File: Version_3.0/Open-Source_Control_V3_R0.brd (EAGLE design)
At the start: 121.9 x 129.5 mm, 353 parts, among them IC10 MCP6002SMT, IC11 MCP6002SMT, IC12 MCP6002SMT, IC14 MCP6002SMT, IC2 ULN2003AD, IC4 74HC165D, IC5 74HC165D, J24 6p-2.54, K1 G5LE-14-CF DC24, K2 G5LE-14-CF DC24, K3 G5LE-14-CF DC24, K4 G5LE-14-CF DC24, Q1 MMBT2907, T4 DA2304-AL, U1 OSD3358-512M-ICB, U16 AT97SC3205T-G3M4400B, U2 TPD4S012_DRY_6_P1_M, U27 LAN8710, U28 TCAN1051HV, U29 MAX3483EESA+T, U4 APX811-31UGSOT, U40 ISO3086TDW, U5 TLVH431, U6 SN74LVC2G241_DCU_8, X1 10118194-0001LF, X10 MC4, X11 MC4, X12 MC4, X2 J0011D01BNL, X21 MC12, X24 MSTBA2, X3 MC4, X31 MC4, X4 CTI-JTAG, X41 MSTBA3, X5 DM3CS-SF, X6 6p-2.54, X7 TH-2X10, X8 TH-2X10, X9 5600200420, Y7 ECS-250-12-30-GN-TR

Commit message: Add files via upload
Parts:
- renumbered H4 to MTG4
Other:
- board text added: "Control v3"
- board text removed: "Building Control v3"
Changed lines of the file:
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@@
 <text x="50.8" y="0.635" size="1.016" layer="21" font="vector" ratio="12">Rev 0</text>
 <text x="40.64" y="4.318" size="1.27" layer="21" ratio="15">Open-Source</text>
-<text x="40.64" y="2.54" size="1.27" layer="21" ratio="15">Building Control v3</text>
+<text x="40.64" y="2.54" size="1.27" layer="21" ratio="15">Control v3</text>
 <wire x1="95.25" y1="107.95" x2="95.25" y2="102.87" width="0.4064" layer="21"/>
 <wire x1="95.25" y1="102.87" x2="90.17" y2="102.87" width="0.4064" layer="21"/>
@@
 </element>
 <element name="D402" library="OSD3358-SM-RED Platform" package="EIA-STD" value="LTST-C191KGKT" x="20.828" y="108.585" smashed="yes" rot="R90">
-<attribute name="NAME" x="20.8534" y="107.1372" size="0.8128" layer="25" align="top-center"/>
+<attribute name="NAME" x="20.828" y="110.0328" size="0.8128" layer="25" align="bottom-center"/>
 <attribute name="VALUE" x="20.1676" y="108.585" size="0.254" layer="27" rot="R90" align="bottom-center"/>
 </element>
 <element name="D401" library="OSD3358-SM-RED Platform" package="EIA-STD" value="LTST-C191KRKT" x="18.796" y="108.585" smashed="yes" rot="R90">
-<attribute name="NAME" x="18.796" y="107.1372" size="0.8128" layer="25" align="top-right"/>
+<attribute name="NAME" x="18.796" y="110.0328" size="0.8128" layer="25" align="bottom-right"/>
 <attribute name="VALUE" x="19.4564" y="108.585" size="0.254" layer="27" rot="R90" align="top-center"/>
 </element>
@@
 <attribute name="POPULARITY" value="0" x="36.195" y="125.095" size="1.778" layer="27" display="off"/>
 </element>
-<element name="H4" library="holes" library_urn="urn:adsk.eagle:library:237" package="3,6-PAD" package3d_urn="urn:adsk.eagle:package:14284/1" value="MOUNT-PAD-ROUND3.6" x="85.725" y="125.095" smashed="yes">
+<element name="MTG4" library="holes" library_urn="urn:adsk.eagle:library:237" package="3,6-PAD" package3d_urn="urn:adsk.eagle:package:14284/1" value="MOUNT-PAD-ROUND3.6" x="85.725" y="125.095" smashed="yes">
 <attribute name="POPULARITY" value="0" x="85.725" y="125.095" size="1.778" layer="27" display="off"/>
 </element>
@@
 <contactref element="MTG1" pad="B3,6"/>
 <contactref element="MTG2" pad="B3,6"/>
-<contactref element="H4" pad="B3,6"/>
+<contactref element="MTG4" pad="B3,6"/>
 <contactref element="MTG3" pad="B3,6"/>
 </signal>

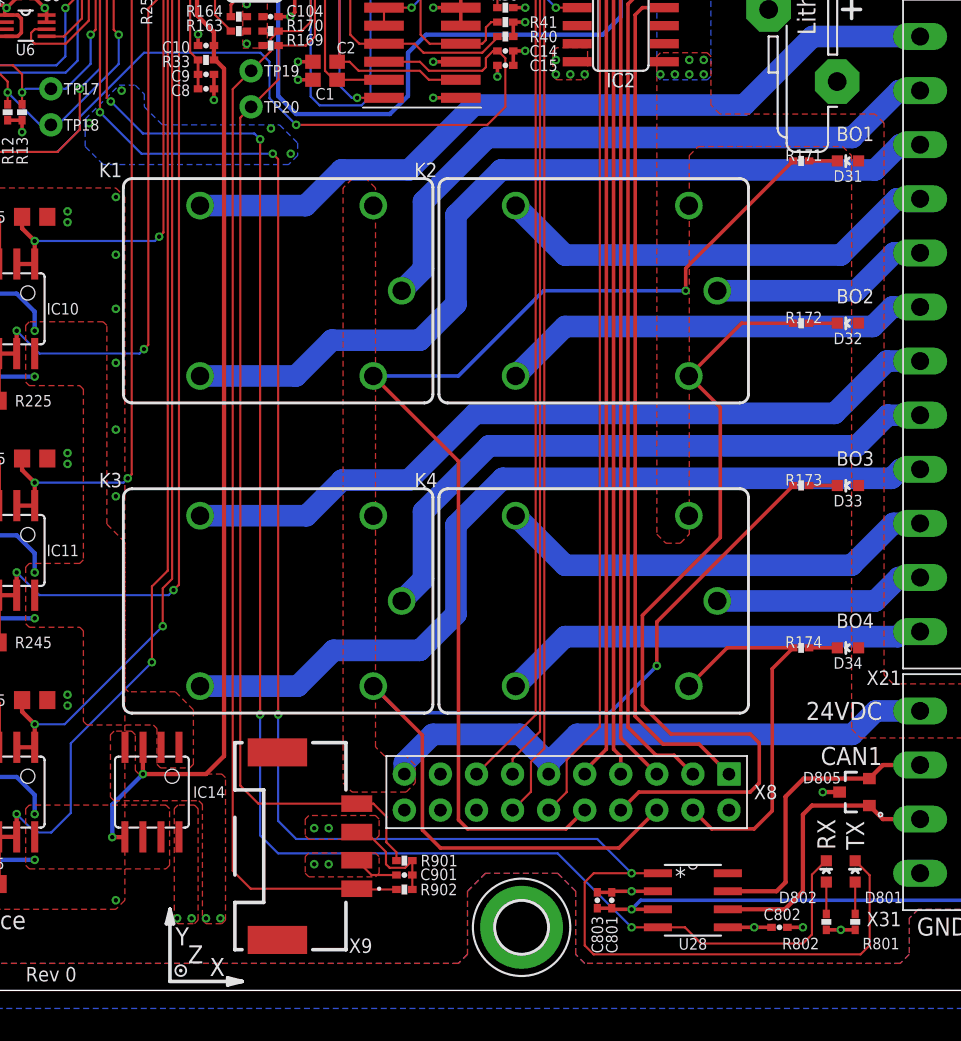
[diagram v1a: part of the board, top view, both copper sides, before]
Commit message: Add files via upload
Fixed CAN1_TXD CAN1_RXD criss-crossed
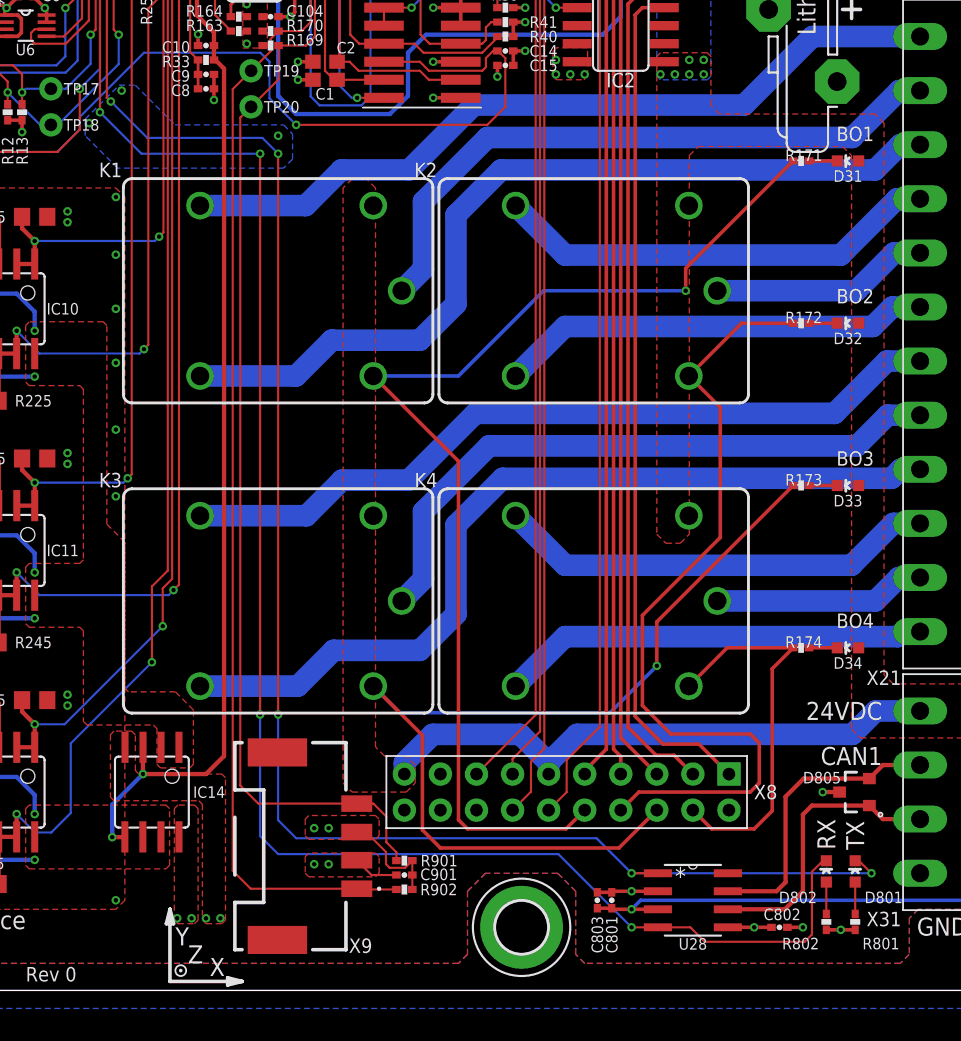
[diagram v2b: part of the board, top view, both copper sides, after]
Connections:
- net CAN1_RXD: now also U1.W7; no longer U1.Y7
- net CAN1_TXD: now also U1.Y7; no longer U1.W7
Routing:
- net CAN1_TXD: track 141.5 -> 122.5 mm, vias 4 -> 5
- net CAN1_RXD: track 124.2 -> 126.2 mm
- net GND: vias 198 -> 197
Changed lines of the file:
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@@
 <vertex x="70.739" y="9.6774"/>
 </polygon>
-<via x="68.072" y="60.706" extent="1-16" drill="0.3048"/>
+<via x="68.58" y="60.198" extent="1-16" drill="0.3048"/>
 <via x="55.2704" y="61.087" extent="1-16" drill="0.3048"/>
-<via x="69.469" y="58.928" extent="1-16" drill="0.3048"/>
 <wire x1="93.472" y1="6.985" x2="95.3262" y2="6.985" width="0.254" layer="1"/>
 <wire x1="93.472" y1="6.985" x2="92.1512" y2="6.985" width="0.254" layer="1"/>
@@
 <vertex x="57.3786" y="63.754"/>
 <vertex x="58.5216" y="63.754"/>
-<vertex x="59.1566" y="63.119"/>
-<vertex x="59.1566" y="62.23"/>
-<vertex x="60.4266" y="60.96"/>
-<vertex x="68.6816" y="60.96"/>
-<vertex x="69.9516" y="59.69"/>
-<vertex x="69.9516" y="58.801"/>
-<vertex x="69.3166" y="58.166"/>
-<vertex x="56.261" y="58.166"/>
-<vertex x="54.991" y="59.436"/>
+<vertex x="61.3156" y="60.96"/>
+<vertex x="68.961" y="60.96"/>
+<vertex x="69.596" y="60.325"/>
+<vertex x="69.596" y="58.547"/>
+<vertex x="68.961" y="57.912"/>
+<vertex x="57.277" y="57.912"/>
+<vertex x="54.991" y="60.198"/>
 <vertex x="54.991" y="61.3664"/>
 </polygon>
@@
 <wire x1="51.435" y1="67.69608125" x2="52.2732" y2="67.69608125" width="0.1524" layer="1"/>
 </signal>
-<signal name="CAN1_TXD">
-<contactref element="U28" pad="1"/>
+<signal name="CAN1_RXD">
 <contactref element="U1" pad="W7"/>
 <wire x1="56.515" y1="79.375" x2="56.515" y2="79.3496" width="0.1524" layer="1"/>
 <wire x1="56.515" y1="79.3496" x2="56.0324" y2="78.867" width="0.1524" layer="1"/>
-<via x="68.199" y="58.928" extent="1-16" drill="0.3048"/>
-<via x="93.472" y="8.255" extent="1-16" drill="0.3048"/>
-<wire x1="95.3262" y1="8.255" x2="93.472" y2="8.255" width="0.1524" layer="1"/>
-<via x="68.58" y="19.431" extent="1-16" drill="0.3048"/>
-<wire x1="93.472" y1="8.255" x2="91.059" y2="10.668" width="0.1524" layer="16"/>
-<wire x1="91.059" y1="10.668" x2="69.85" y2="10.668" width="0.1524" layer="16"/>
-<wire x1="69.85" y1="10.668" x2="68.58" y2="11.938" width="0.1524" layer="16"/>
-<wire x1="68.58" y1="11.938" x2="68.58" y2="19.431" width="0.1524" layer="16"/>
-<wire x1="68.58" y1="58.547" x2="68.58" y2="19.431" width="0.1524" layer="1"/>
-<contactref element="D801" pad="2"/>
-<wire x1="93.472" y1="8.255" x2="90.805" y2="8.255" width="0.1524" layer="1"/>
-<wire x1="90.805" y1="8.255" x2="90.17" y2="7.62" width="0.1524" layer="1"/>
-<wire x1="90.17" y1="7.62" x2="90.17" y2="3.175" width="0.1524" layer="1"/>
-<wire x1="90.17" y1="3.175" x2="90.805" y2="2.54" width="0.1524" layer="1"/>
-<wire x1="90.805" y1="2.54" x2="109.601" y2="2.54" width="0.1524" layer="1"/>
-<wire x1="109.601" y1="2.54" x2="110.236" y2="3.175" width="0.1524" layer="1"/>
-<wire x1="110.236" y1="3.175" x2="110.236" y2="8.1153" width="0.1524" layer="1"/>
-<wire x1="110.236" y1="8.1153" x2="109.22" y2="9.1313" width="0.1524" layer="1"/>
+<via x="67.31" y="58.928" extent="1-16" drill="0.3048"/>
+<via x="93.472" y="4.445" extent="1-16" drill="0.3048"/>
+<via x="67.31" y="19.431" extent="1-16" drill="0.3048"/>
 <via x="56.0324" y="61.849" extent="1-16" drill="0.3048"/>
 <wire x1="56.0324" y1="78.867" x2="56.0324" y2="61.849" width="0.1524" layer="1"/>
-<wire x1="68.58" y1="58.547" x2="68.199" y2="58.928" width="0.1524" layer="1"/>
 <wire x1="56.0324" y1="61.849" x2="58.9534" y2="58.928" width="0.1524" layer="16"/>
-<wire x1="58.9534" y1="58.928" x2="68.199" y2="58.928" width="0.1524" layer="16"/>
-</signal>
-<signal name="CAN1_RXD">
+<wire x1="58.9534" y1="58.928" x2="67.31" y2="58.928" width="0.1524" layer="16"/>
 <contactref element="U28" pad="4"/>
+<contactref element="D802" pad="2"/>
+<wire x1="105.664" y1="3.429" x2="106.172" y2="3.937" width="0.1524" layer="1"/>
+<wire x1="98.6282" y1="3.429" x2="105.664" y2="3.429" width="0.1524" layer="1"/>
+<wire x1="67.31" y1="58.928" x2="67.31" y2="19.431" width="0.1524" layer="1"/>
+<wire x1="88.3158" y1="9.6012" x2="68.58" y2="9.6012" width="0.1524" layer="16"/>
+<wire x1="68.58" y1="9.6012" x2="67.31" y2="10.8712" width="0.1524" layer="16"/>
+<wire x1="67.31" y1="10.8712" x2="67.31" y2="19.431" width="0.1524" layer="16"/>
+<wire x1="93.472" y1="4.445" x2="88.3158" y2="9.6012" width="0.1524" layer="16"/>
+<wire x1="95.3262" y1="4.445" x2="97.6122" y2="4.445" width="0.1524" layer="1"/>
+<wire x1="97.6122" y1="4.445" x2="98.6282" y2="3.429" width="0.1524" layer="1"/>
+<wire x1="93.472" y1="4.445" x2="95.3262" y2="4.445" width="0.1524" layer="1"/>
+<wire x1="106.9467" y1="9.1313" x2="107.188" y2="9.1313" width="0.1524" layer="1"/>
+<wire x1="106.172" y1="3.937" x2="106.172" y2="8.3566" width="0.1524" layer="1"/>
+<wire x1="106.172" y1="8.3566" x2="106.9467" y2="9.1313" width="0.1524" layer="1"/>
+</signal>
+<signal name="CAN1_TXD">
 <contactref element="U1" pad="Y7"/>
-<via x="67.31" y="59.944" extent="1-16" drill="0.3048"/>
-<via x="93.472" y="4.445" extent="1-16" drill="0.3048"/>
-<wire x1="95.3262" y1="4.445" x2="93.472" y2="4.445" width="0.1524" layer="1"/>
-<via x="67.31" y="19.431" extent="1-16" drill="0.3048"/>
-<wire x1="88.265" y1="9.652" x2="68.58" y2="9.652" width="0.1524" layer="16"/>
-<wire x1="68.58" y1="9.652" x2="67.31" y2="10.922" width="0.1524" layer="16"/>
-<wire x1="67.31" y1="10.922" x2="67.31" y2="19.431" width="0.1524" layer="16"/>
-<wire x1="93.472" y1="4.445" x2="88.265" y2="9.652" width="0.1524" layer="16"/>
-<wire x1="67.31" y1="59.944" x2="67.31" y2="19.431" width="0.1524" layer="1"/>
-<contactref element="D802" pad="2"/>
-<wire x1="95.3262" y1="4.445" x2="97.2312" y2="4.445" width="0.1524" layer="1"/>
-<wire x1="97.2312" y1="4.445" x2="98.3742" y2="3.302" width="0.1524" layer="1"/>
-<wire x1="98.3742" y1="3.302" x2="105.537" y2="3.302" width="0.1524" layer="1"/>
-<wire x1="105.537" y1="3.302" x2="106.172" y2="3.937" width="0.1524" layer="1"/>
-<wire x1="106.172" y1="3.937" x2="106.172" y2="8.1534" width="0.1524" layer="1"/>
-<wire x1="106.172" y1="8.1534" x2="107.1499" y2="9.1313" width="0.1524" layer="1"/>
-<wire x1="107.1499" y1="9.1313" x2="107.188" y2="9.1313" width="0.1524" layer="1"/>
+<via x="68.58" y="58.928" extent="1-16" drill="0.3048"/>
+<via x="93.472" y="8.255" extent="1-16" drill="0.3048"/>
+<via x="68.58" y="19.431" extent="1-16" drill="0.3048"/>
 <via x="56.7944" y="62.611" extent="1-16" drill="0.3048"/>
 <wire x1="56.515" y1="78.105" x2="56.515" y2="62.8904" width="0.1524" layer="1"/>
 <wire x1="56.515" y1="62.8904" x2="56.7944" y2="62.611" width="0.1524" layer="1"/>
-<wire x1="56.7944" y1="62.611" x2="59.055" y2="60.3504" width="0.1524" layer="16"/>
-<wire x1="66.9036" y1="60.3504" x2="67.31" y2="59.944" width="0.1524" layer="16"/>
-<wire x1="59.055" y1="60.3504" x2="66.9036" y2="60.3504" width="0.1524" layer="16"/>
+<wire x1="56.7944" y1="62.611" x2="59.3598" y2="60.0456" width="0.1524" layer="16"/>
+<wire x1="67.4624" y1="60.0456" x2="68.58" y2="58.928" width="0.1524" layer="16"/>
+<wire x1="59.3598" y1="60.0456" x2="67.4624" y2="60.0456" width="0.1524" layer="16"/>
+<contactref element="U28" pad="1"/>
+<contactref element="D801" pad="2"/>
+<wire x1="68.58" y1="58.928" x2="68.58" y2="19.431" width="0.1524" layer="1"/>
+<wire x1="68.58" y1="19.431" x2="68.58" y2="11.9888" width="0.1524" layer="16"/>
+<wire x1="68.58" y1="11.9888" x2="69.85" y2="10.7188" width="0.1524" layer="16"/>
+<wire x1="69.85" y1="10.7188" x2="91.0082" y2="10.7188" width="0.1524" layer="16"/>
+<wire x1="91.0082" y1="10.7188" x2="93.472" y2="8.255" width="0.1524" layer="16"/>
+<via x="110.363" y="8.255" extent="1-16" drill="0.3048"/>
+<wire x1="110.363" y1="8.255" x2="93.472" y2="8.255" width="0.1524" layer="16"/>
+<wire x1="93.472" y1="8.255" x2="95.3262" y2="8.255" width="0.1524" layer="1"/>
+<wire x1="110.363" y1="8.255" x2="109.4867" y2="9.1313" width="0.1524" layer="1"/>
+<wire x1="109.4867" y1="9.1313" x2="109.22" y2="9.1313" width="0.1524" layer="1"/>
 </signal>
 <signal name="USB0_P">

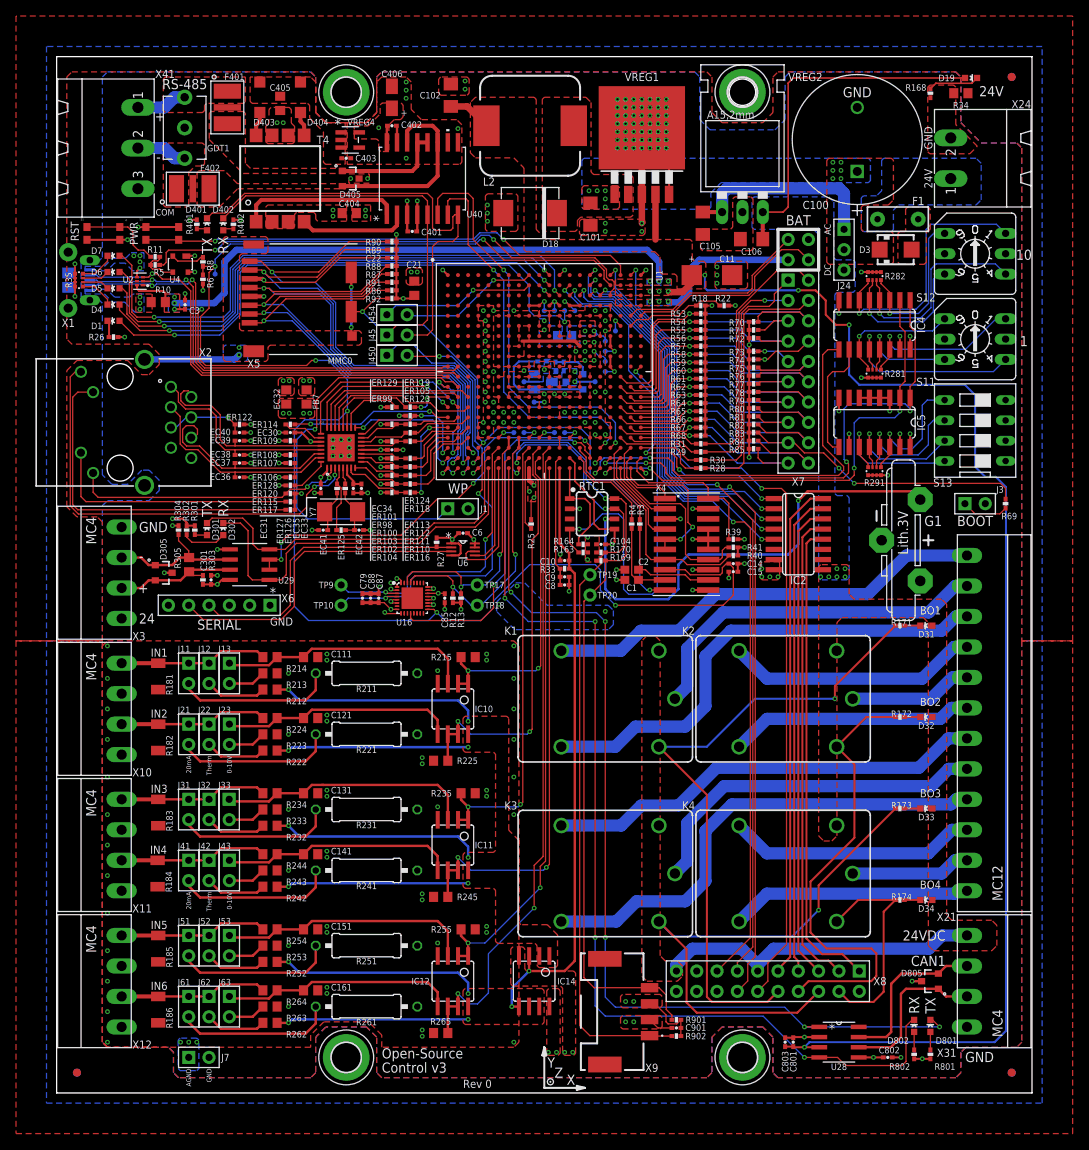
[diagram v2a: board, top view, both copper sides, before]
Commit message: Added 6th B-output BO_6
Added 6th B-output BO_6 to expansion header. Now a total of 6 relay outputs are possible
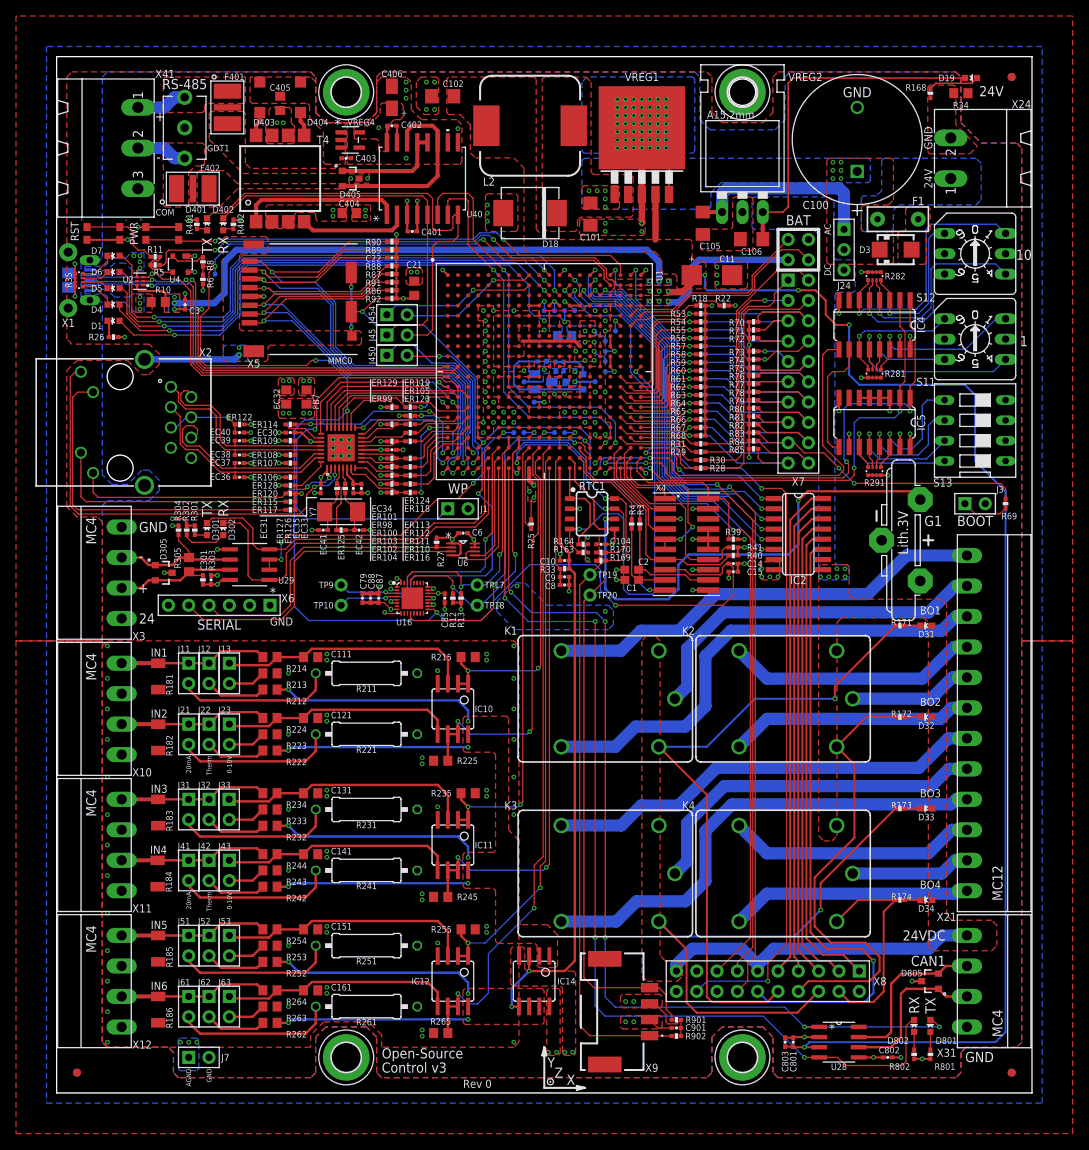
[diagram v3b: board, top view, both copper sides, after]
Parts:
- moved C102 1.02 mm to (48.3, 124.6), turned to 180 degrees
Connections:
- new net BO6_AUTO: IC2.11, X8.12
- net GPIO1_16: now also IC2.6, U1.A13; no longer U1.B14
- net PMIC_NRESET: now also X8.18; no longer X8.12
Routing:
- net BO6_AUTO: track 0.00 -> 78.0 mm, vias 0 -> 1
- net GPIO1_16: track 0.00 -> 50.0 mm, vias 0 -> 2
- net PMIC_NRESET: track 105.5 -> 113.2 mm, vias 2 -> 3
- net VDD_5V: track 173.3 -> 167.1 mm
- net BO2: track 58.0 -> 57.0 mm
- net GND: vias 197 -> 199
